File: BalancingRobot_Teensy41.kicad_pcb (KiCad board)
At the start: 2 copper layers, 19 parts, among them J1 Conn_01x06_Socket, J2 Conn_01x04_Socket, J3 Conn_01x02_Socket, J4 Conn_01x06_Socket, J5 Conn_01x06_Socket, U1 Teensy4.1, U2 ICM20948_Carrier_Board, U3 DRV8874_Carrier, U4 DRV8874_Carrier

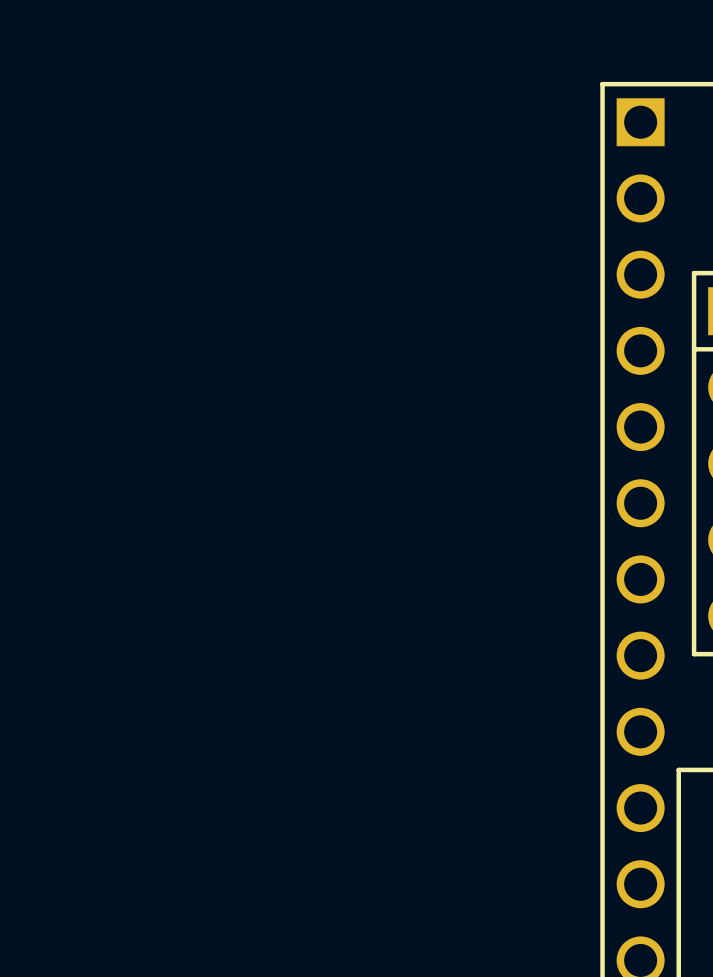
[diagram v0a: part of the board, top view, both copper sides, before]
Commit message: Added bulk caps for VIN on Teensy and Motor Controllers
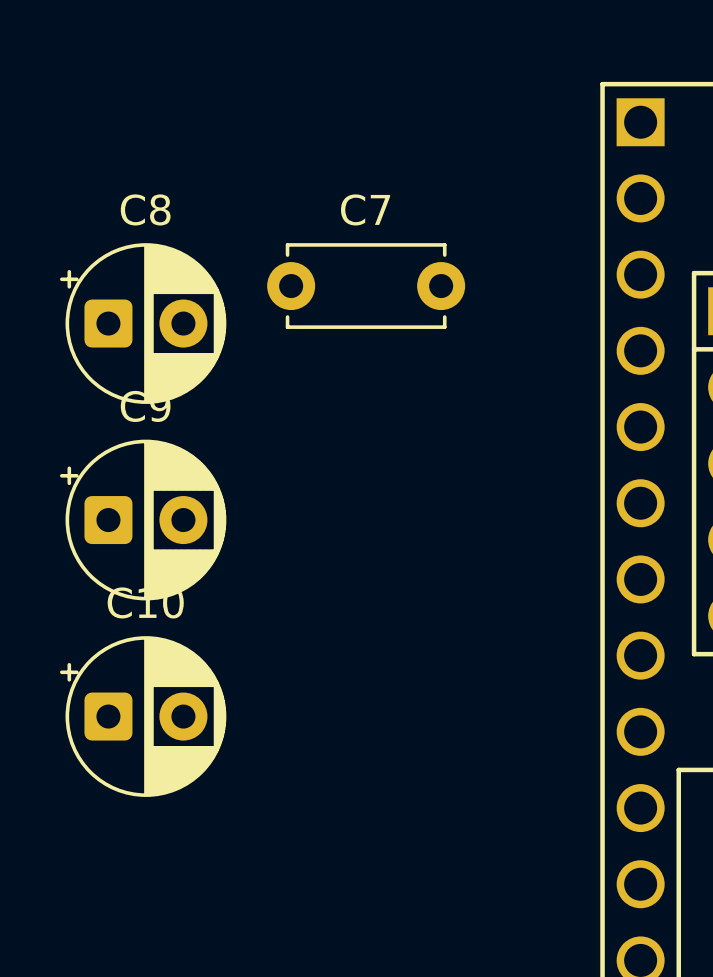
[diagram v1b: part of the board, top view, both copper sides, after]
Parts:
- added C10: 100u, Capacitor_THT:CP_Radial_D5.0mm_P2.50mm, F.Cu at (111.2, 81.5)
- added C7: 100n, Capacitor_THT:C_Disc_D5.0mm_W2.5mm_P5.00mm, F.Cu at (117.3, 67.2)
- added C8: 10u, Capacitor_THT:CP_Radial_D5.0mm_P2.50mm, F.Cu at (111.2, 68.4)
- added C9: 100u, Capacitor_THT:CP_Radial_D5.0mm_P2.50mm, F.Cu at (111.2, 75.0)

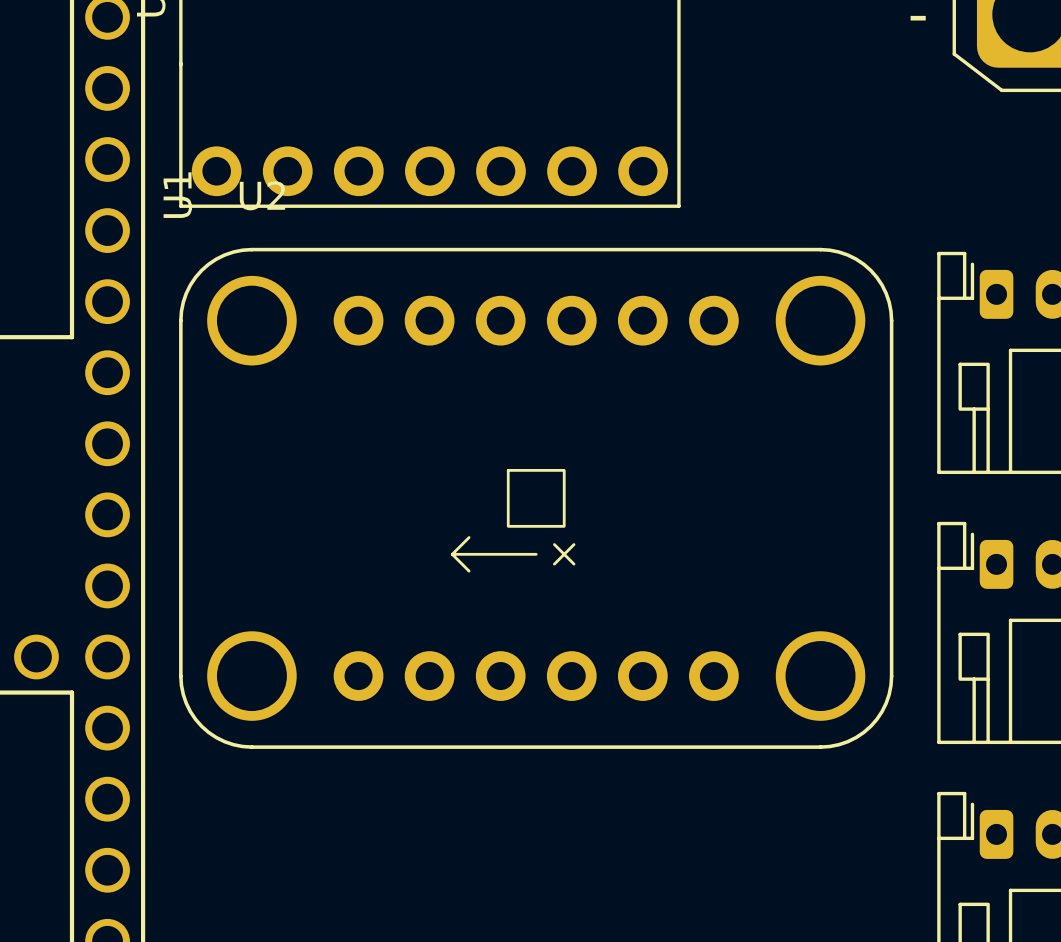
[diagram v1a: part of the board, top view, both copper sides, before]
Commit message: Split busy schematic into subpages. Mainly moved ICM20948 and the two motor controllers to inidividual pages
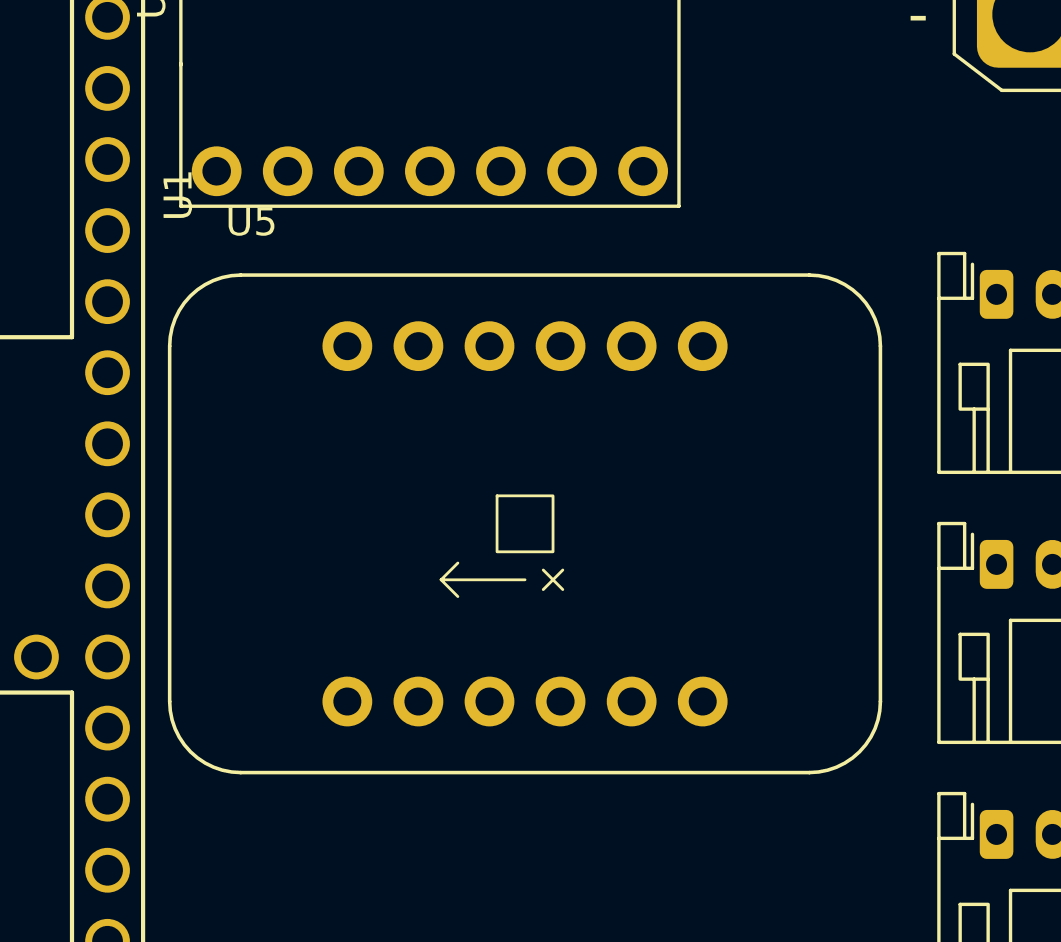
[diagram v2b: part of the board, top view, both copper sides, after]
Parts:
- removed U2: ICM20948_Carrier_Board, Adafruit_ICM20948:ICM20948_Carrier
- added U5: ICM20948_Carrier_Board, Adafruit_ICM20948:ICM20948_Carrier, F.Cu at (159.2, 102.7)

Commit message: Started with routing
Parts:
- J1: value Conn_01x06_Socket -> PM02D
- J2: value Conn_01x04_Socket -> UART
- J3: value Conn_01x02_Socket -> XT30
- J4: value Conn_01x06_Socket -> MOT-A
- J5: value Conn_01x06_Socket -> MOT-B
- moved J2 75.1 mm to (105.2, 97.2), turned to -90 degrees
- moved J1 72.9 mm to (105.5, 76.2), turned to -90 degrees
- moved J4 71.6 mm to (105.2, 114.8), turned to -90 degrees
- moved C1 68.9 mm to (119.5, 110.5), turned to 90 degrees
- moved R2 65.5 mm to (129.8, 110.6), turned to 90 degrees
- moved C10 64.5 mm to (161.8, 121.5)
- moved R1 64.0 mm to (127.5, 102.9), turned to -90 degrees
- moved C2 63.4 mm to (123.2, 110.5), turned to 90 degrees
- moved U3 62.9 mm to (122.0, 120.0)
- moved J3 60.1 mm to (152.5, 139.2), turned to 180 degrees
- moved C9 52.1 mm to (136.5, 120.5), turned to -90 degrees
- moved C3 42.9 mm to (175.2, 110.8), turned to 90 degrees
- moved R4 42.8 mm to (185.8, 111.1), turned to 90 degrees
- moved U4 42.6 mm to (178.0, 120.0)
- moved C4 39.8 mm to (178.8, 110.8), turned to 90 degrees
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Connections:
- U1 pad 66: unconnected-(U1-D--Pad66) -> (no net)
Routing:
- net +12V: track 0.00 -> 85.6 mm
- net PM02_SDA: track 0.00 -> 47.0 mm
- net PM02_SCL: track 0.00 -> 43.6 mm
- net ICM20948_SCL: track 0.00 -> 37.2 mm
- net ICM20948_INT: track 0.00 -> 32.7 mm
- net Net-(J4-M-): track 0.00 -> 31.0 mm
- net Net-(J4-M+): track 0.00 -> 29.0 mm
- net +5V: track 0.00 -> 27.0 mm
- net ICM20948_SDO: track 0.00 -> 25.1 mm
- net ICM20948_CS: track 0.00 -> 19.9 mm
- net ICM20948_SDI: track 0.00 -> 18.7 mm
- net Net-(J5-M-): track 0.00 -> 2.99 mm
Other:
- board outline added: 102 x 84 mm

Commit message: Almost completed with routing
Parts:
- added H1: MountingHole_Pad, MountingHole:MountingHole_3.2mm_M3_Pad_Via, F.Cu at (104.0, 59.0)
- added H2: MountingHole_Pad, MountingHole:MountingHole_3.2mm_M3_Pad_Via, F.Cu at (194.0, 59.0)
- added H3: MountingHole_Pad, MountingHole:MountingHole_3.2mm_M3_Pad_Via, F.Cu at (104.0, 140.9)
- added H4: MountingHole_Pad, MountingHole:MountingHole_3.2mm_M3_Pad_Via, F.Cu at (194.0, 141.0)
- moved J2 89.4 mm to (192.8, 79.6), turned to 90 degrees
- moved C5 46.3 mm to (132.8, 100.9), turned to 90 degrees
- moved C2 21.9 mm to (101.4, 112.5), turned to 0 degrees
- moved J5 20.1 mm to (192.4, 104.9)
- moved J4 19.8 mm to (105.2, 95.0)
- moved C9 19.8 mm to (122.3, 134.4)
- moved C6 19.4 mm to (164.3, 102.0), turned to 90 degrees
- moved C10 19.2 mm to (173.8, 136.5), turned to 180 degrees
- moved R4 14.7 mm to (172.2, 105.3), turned to 180 degrees
- moved R1 14.7 mm to (113.0, 105.3), turned to 0 degrees
- moved C4 14.6 mm to (188.1, 122.0), turned to -90 degrees
- moved C3 13.2 mm to (188.0, 114.1), turned to -90 degrees
- moved C1 12.3 mm to (110.1, 118.5), turned to 180 degrees
- moved R2 8.52 mm to (123.0, 105.3), turned to 0 degrees
- moved C7 6.06 mm to (109.6, 68.7), turned to 90 degrees
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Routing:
- net +3V3: track 0.00 -> 236.9 mm
- net MOTA_FAULT: track 0.00 -> 105.8 mm, vias 0 -> 1
- net UART_COMP_RX: track 0.00 -> 82.6 mm
- net MOTB_FAULT: track 0.00 -> 74.6 mm
- net MOTB_CUR: track 0.00 -> 74.0 mm, vias 0 -> 1
- net UART_COMP_TX: track 0.00 -> 73.3 mm
- net MOTB_DIR: track 0.00 -> 67.9 mm
- net MOTA_SLEEP: track 0.00 -> 66.9 mm
- net MOTB_PWM: track 0.00 -> 66.7 mm, vias 0 -> 1
- net MOTA_CUR: track 0.00 -> 53.9 mm
- net MOTB_SLEEP: track 0.00 -> 48.3 mm
- net MOTA_PWM: track 0.00 -> 43.3 mm
- net MOTA_DIR: track 0.00 -> 40.3 mm
- net ENC_A_PH_B: track 0.00 -> 31.3 mm
- net Net-(J5-M-): track 2.99 -> 31.7 mm
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- added copper zone on B.Cu, net GND
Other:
- board size 102 x 84 mm -> 100 x 92 mm

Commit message: Added some updates
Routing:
- net MOTA_SLEEP: track 66.9 -> 71.6 mm
- net MOTB_CUR: track 74.0 -> 77.8 mm
- net UART_COMP_TX: track 73.3 -> 74.1 mm
- net ENC_B_PH_B: track 23.4 -> 23.9 mm
- net GND: vias 0 -> 118
- net (no net): vias 25 -> 0
- added copper zone on F.Cu, net GND
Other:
- board text added: "A"
- board text added: "B"
- board text added: "GND"
- board text added: "M+"
- board text added: "M-"
- board text added: "VCC"
